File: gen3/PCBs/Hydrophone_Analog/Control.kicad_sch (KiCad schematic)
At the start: 9 parts, among them U701 MCP23017x-x-SS, U702 MCP23017x-x-SS, U703 MCP23017x-x-SS

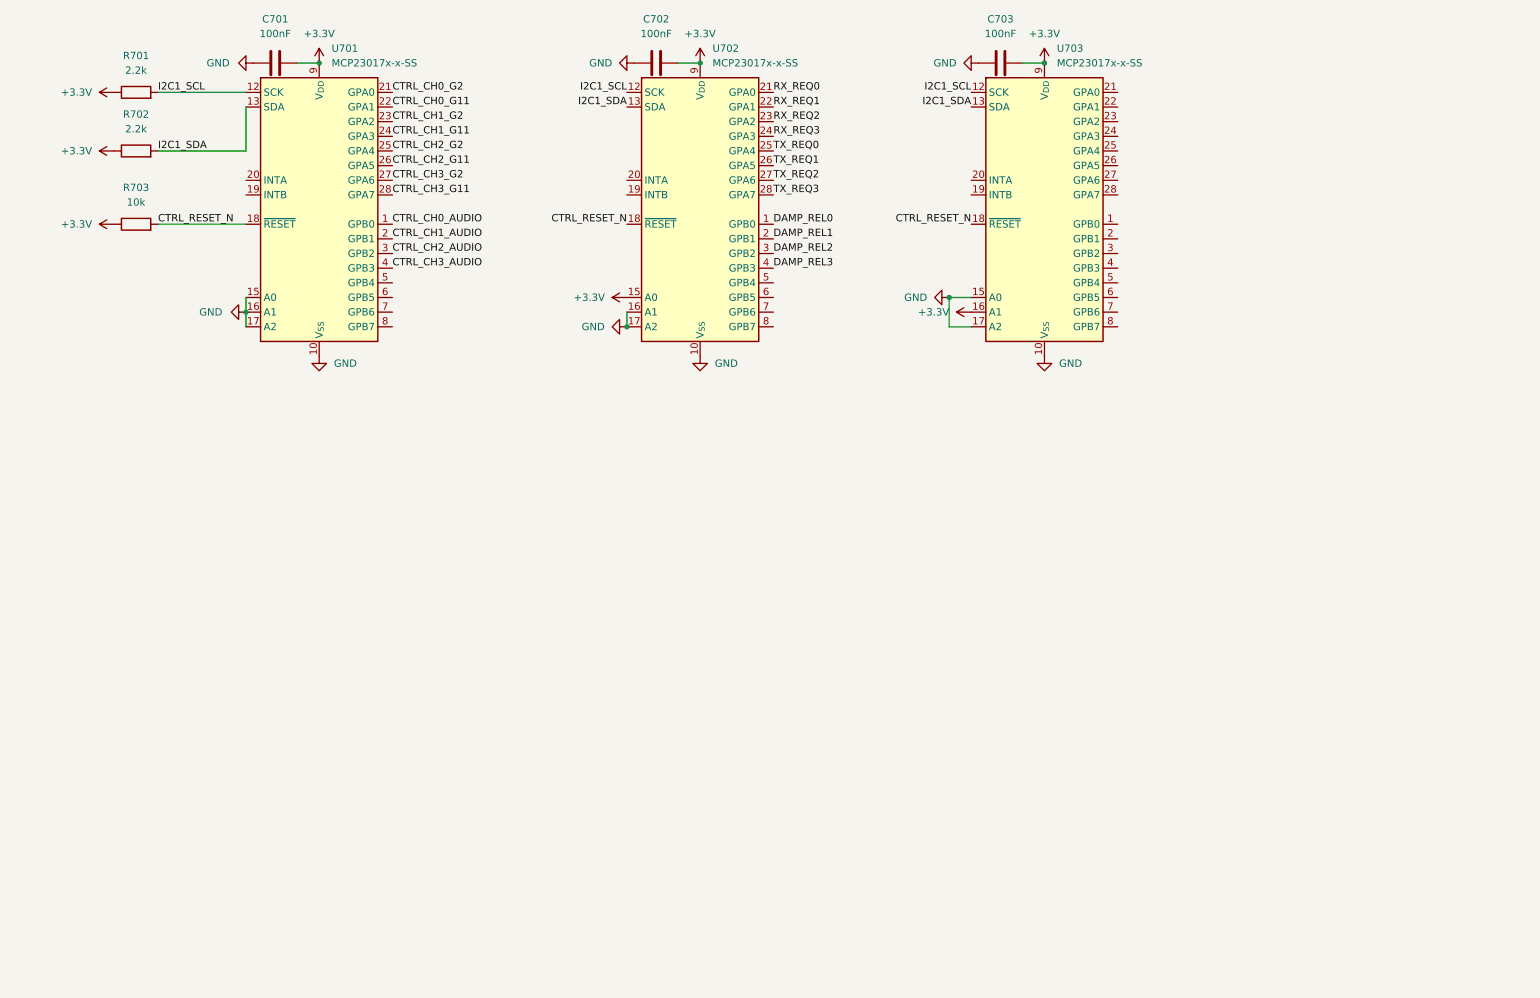
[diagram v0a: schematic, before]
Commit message: Finalized Hydrophone Analog and Power board schematics and power tree
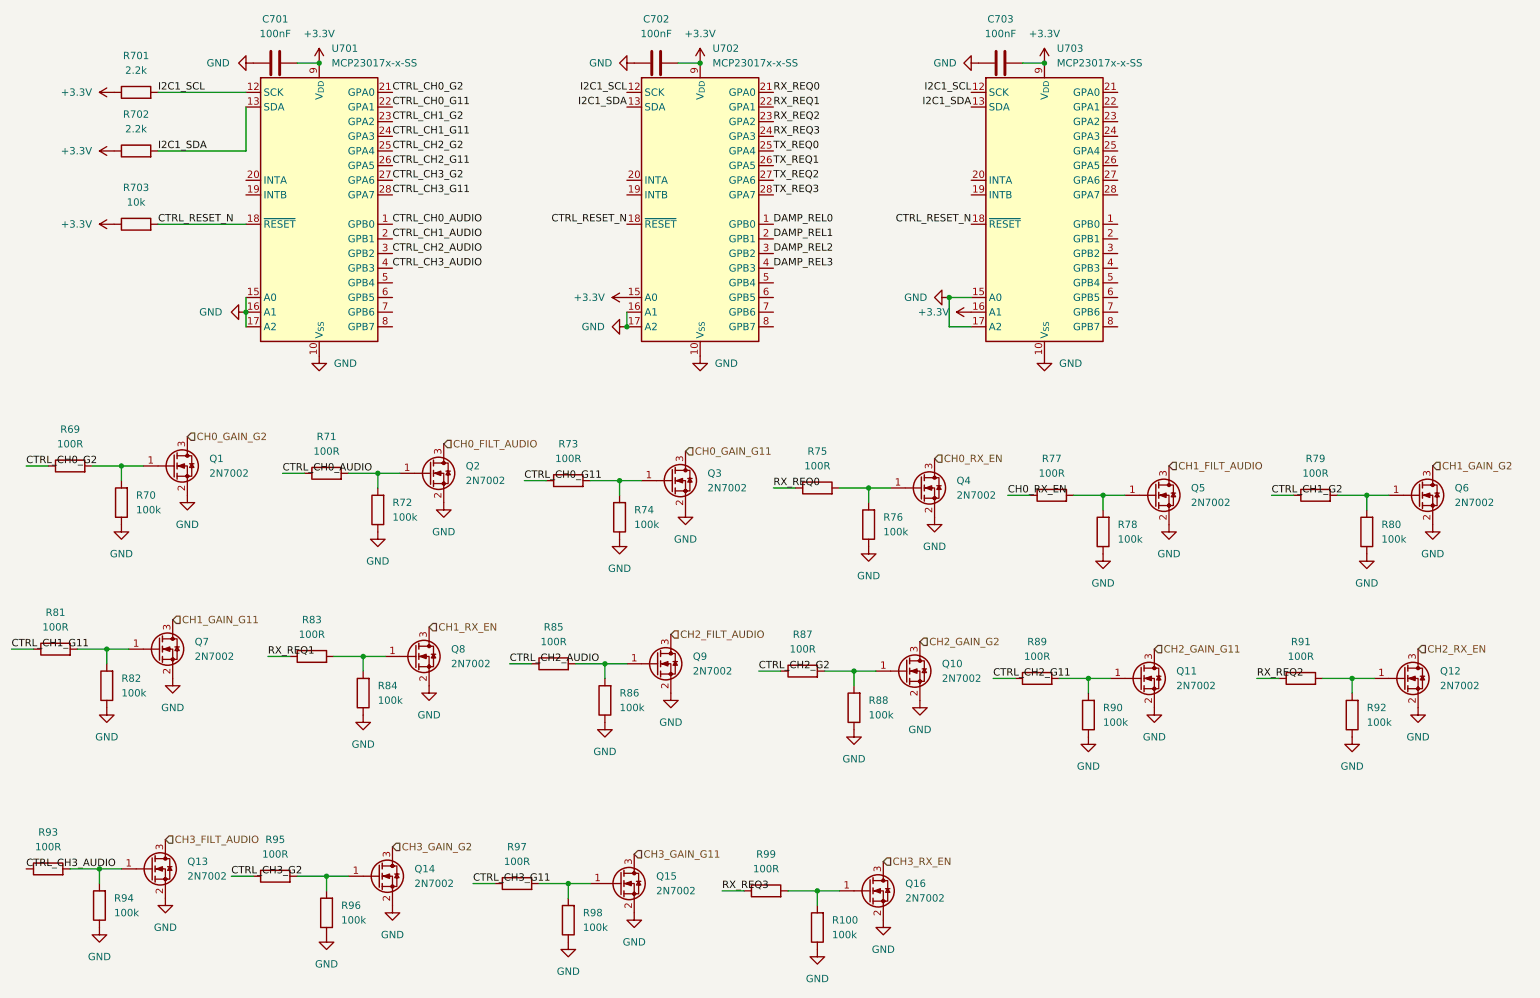
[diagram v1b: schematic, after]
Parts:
- added Q1, Q10, Q11, Q12, Q13, Q14, Q15, Q16, Q2, Q3, Q4, Q5, Q6, Q7, Q8, Q9: 2N7002, Package_TO_SOT_SMD:SOT-23, symbol Transistor_FET:2N7002
- added R100, R70, R72, R74, R76, R78, R80, R82, R84, R86, R88, R90, R92, R94, R96, R98: 100k, Resistor_SMD:R_0805_2012Metric, symbol Device:R
- added R69, R71, R73, R75, R77, R79, R81, R83, R85, R87, R89, R91, R93, R95, R97, R99: 100R, Resistor_SMD:R_0805_2012Metric, symbol Device:R
- C701, C702, C703: footprint (none) -> Capacitor_SMD:C_0805_2012Metric
- R701, R702, R703: footprint (none) -> Resistor_SMD:R_0805_2012Metric
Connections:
- net CTRL_CH0_AUDIO: now also R71.1
- net CTRL_CH0_G11: now also R73.1
- net CTRL_CH0_G2: now also R69.1
- net CTRL_CH1_G11: now also R81.1
- net CTRL_CH1_G2: now also R79.1
- net CTRL_CH2_AUDIO: now also R85.1
- net CTRL_CH2_G11: now also R89.1
- net CTRL_CH2_G2: now also R87.1
- net CTRL_CH3_AUDIO: now also R93.1
- net CTRL_CH3_G11: now also R97.1
- net CTRL_CH3_G2: now also R95.1
- net GND: now also Q1.2 (S), Q10.2 (S), Q11.2 (S), Q12.2 (S), Q13.2 (S), Q14.2 (S), Q15.2 (S), Q16.2 (S), Q2.2 (S), Q3.2 (S), Q4.2 (S), Q5.2 (S), Q6.2 (S), Q7.2 (S), Q8.2 (S), Q9.2 (S), R100.1, R70.1, R72.1, R74.1, R76.1, R78.1, R80.1, R82.1, R84.1, R86.1, R88.1, R90.1, R92.1, R94.1, R96.1, R98.1
- net RX_REQ0: now also R75.1
- net RX_REQ1: now also R83.1
- net RX_REQ2: now also R91.1
- net RX_REQ3: now also R99.1
- new net: Q1.1 (G), R69.2, R70.2
- new net: Q11.1 (G), R89.2, R90.2
- new net: Q3.1 (G), R73.2, R74.2
- new net: Q16.1 (G), R100.2, R99.2
- new net: Q13.1 (G), R93.2, R94.2
- new net: Q15.1 (G), R97.2, R98.2
- new net: Q14.1 (G), R95.2, R96.2
- new net: Q7.1 (G), R81.2, R82.2
- new net: Q4.1 (G), R75.2, R76.2
- new net: Q2.1 (G), R71.2, R72.2
- new net: Q8.1 (G), R83.2, R84.2
- new net: Q10.1 (G), R87.2, R88.2
- new net: Q6.1 (G), R79.2, R80.2
- new net: Q5.1 (G), R77.2, R78.2
- new net: Q9.1 (G), R85.2, R86.2
- new net: Q12.1 (G), R91.2, R92.2
- new net CH0_FILT_AUDIO: Q2.3 (D)
- new net CH0_GAIN_G11: Q3.3 (D)
- new net CH0_GAIN_G2: Q1.3 (D)
- new net CH0_RX_EN: Q4.3 (D), R77.1
- new net CH1_FILT_AUDIO: Q5.3 (D)
- new net CH1_GAIN_G11: Q7.3 (D)
- new net CH1_GAIN_G2: Q6.3 (D)
- new net CH1_RX_EN: Q8.3 (D)
- new net CH2_FILT_AUDIO: Q9.3 (D)
- new net CH2_GAIN_G11: Q11.3 (D)
- new net CH2_GAIN_G2: Q10.3 (D)
- new net CH2_RX_EN: Q12.3 (D)
- new net CH3_FILT_AUDIO: Q13.3 (D)
- new net CH3_GAIN_G11: Q15.3 (D)
- new net CH3_GAIN_G2: Q14.3 (D)
- new net CH3_RX_EN: Q16.3 (D)

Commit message: fixed labelling issues + power design choices, switched footprints to smaller relays
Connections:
- net CH0_RX_EN: no longer R77.1
- net CTRL_CH1_AUDIO: now also R77.1
